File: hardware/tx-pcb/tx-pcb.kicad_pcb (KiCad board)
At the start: 4 copper layers, 70 x 79.1 mm, 54 parts, among them J1 Conn_To_J1, J2 Conn_To_J2, J3 BLIO, J4 Conn_01x05, J5 Conn_01x04, J6 Conn_01x04, J7 Conn_01x02_Pin, SW1 BOOT0, SW2 RESET, SW3 BTN1, SW4 BTN2, SW5 BTN3, SW6 BTN4, SW7 BTN5, SW9 SW_SPDT, U2 STM32WB55CEUx, X1 Q22FA12800025, X2 ABS07-32.768KHZ-1-T

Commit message: double checked silkscreen labels, fixed incorrect, QOL labeling
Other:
- board text added: "REG IN"
- board text added: "REG OUT"

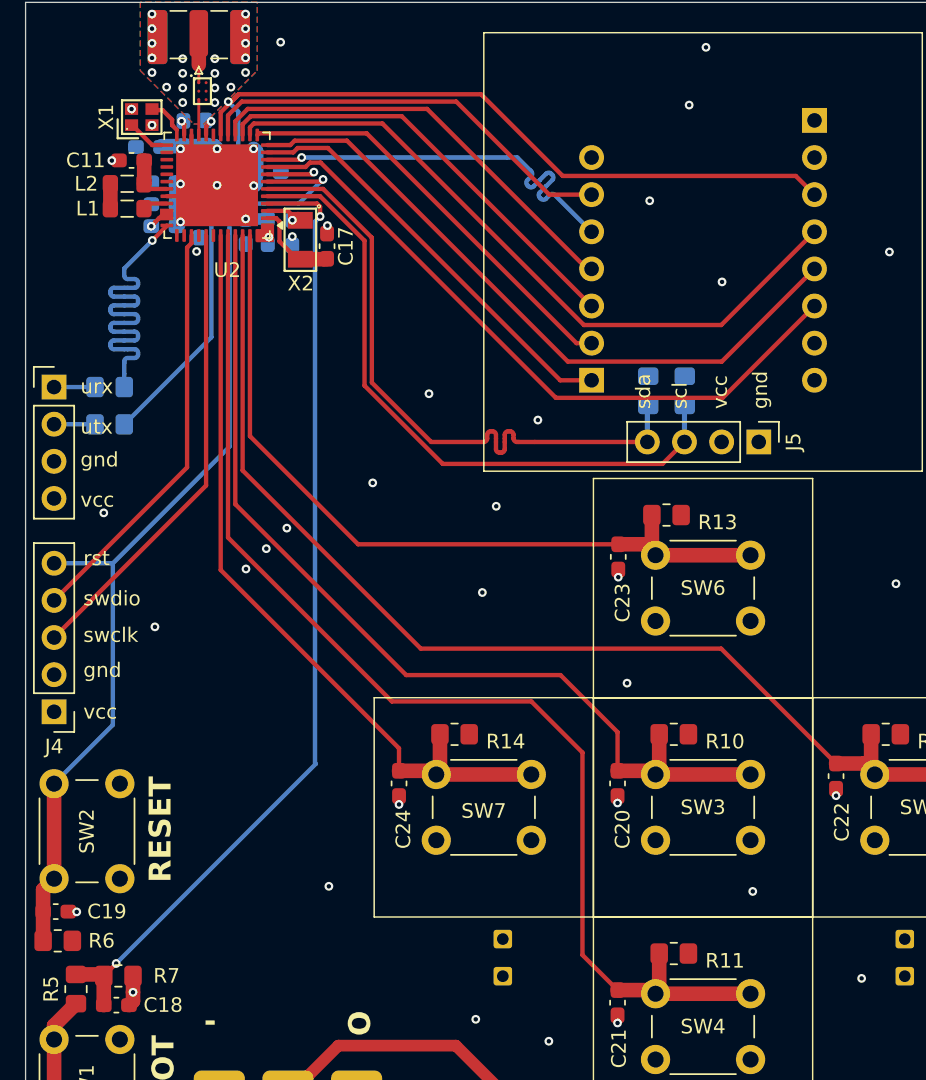
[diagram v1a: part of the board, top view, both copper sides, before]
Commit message: fixed the pinouts to properly match WB55CCU6 CubeMX software options
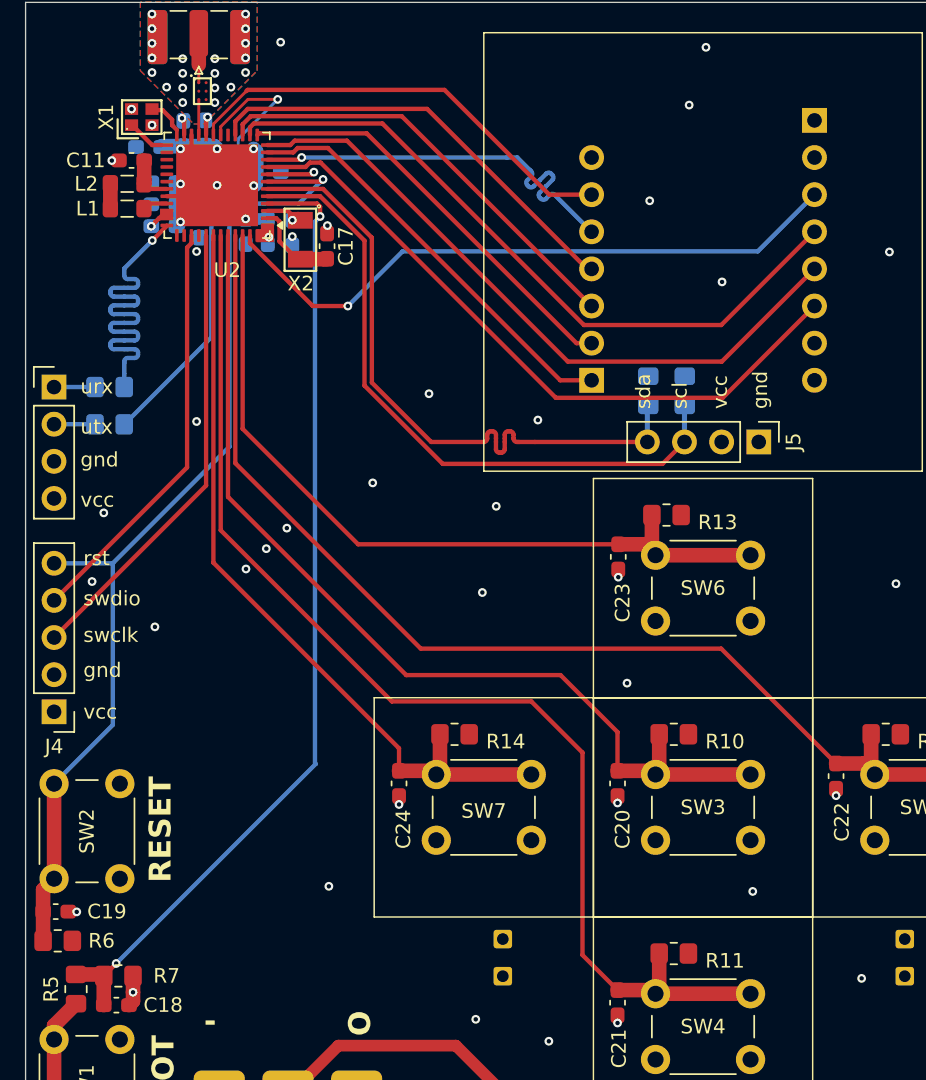
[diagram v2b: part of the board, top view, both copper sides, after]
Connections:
- net /SX1262_RFSW renamed /SX1262_TXEN
- J2 pad 3: /SX1262_RFSW# -> /SX1262_RXEN
- R1 pad 1: Net-(U2-PA10) -> /USART_RX
- R2 pad 1: /SX1262_RFSW# -> /USART_TX
- U2 pad 17: /SX1262_NSS -> unconnected-(U2-PA8-Pad17)
- U2 pad 18: /SX1262_RFSW# -> /USART_TX
- U2 pad 19: unconnected-(U2-PB2-Pad19) -> /SX1262_NSS
- U2 pad 36: Net-(U2-PA10) -> /USART_RX
- U2 pad 37: /USB_DM -> unconnected-(U2-PA11-Pad37)
- U2 pad 38: /USB_DP -> unconnected-(U2-PA12-Pad38)
- U2 pad 42: unconnected-(U2-PA15-Pad42) -> /BTN5
- U2 pad 43: /BTN5 -> /BTN2
- U2 pad 44: /BTN2 -> /BTN1
- U2 pad 45: /BTN1 -> /BTN3
- U2 pad 46: /BTN3 -> /BTN4
- U2 pad 47: /BTN4 -> /SX1262_RXEN
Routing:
- net /SX1262_RFSW#: track 72.1 -> 0.00 mm, vias 1 -> 0
- net /SX1262_RXEN: track 0.00 -> 44.1 mm, vias 0 -> 1
- net /USART_TX: track 2.81 -> 34.6 mm, vias 0 -> 1
- net Net-(U2-PA10): track 27.0 -> 0.00 mm, vias 1 -> 0
- net /USART_RX: track 2.81 -> 29.8 mm, vias 0 -> 1
- net /SX1262_NSS: track 29.2 -> 30.6 mm
- net +3V3: track 6.91 -> 7.29 mm, vias 24 -> 26
